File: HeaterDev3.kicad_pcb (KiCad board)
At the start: 2 copper layers, 101.6 x 76.2 mm, 27 parts, among them J1 USB_C_Receptacle_USB2.0, J9 Conn_01x04_Female, Q1 Q_NMOS_GSD, SW1 SW_SPST, U1 ATSAMD21E18A-MU, U2 FUSB302BMPX, U3 STS-30-DIS, U5 AP2112K-3.3

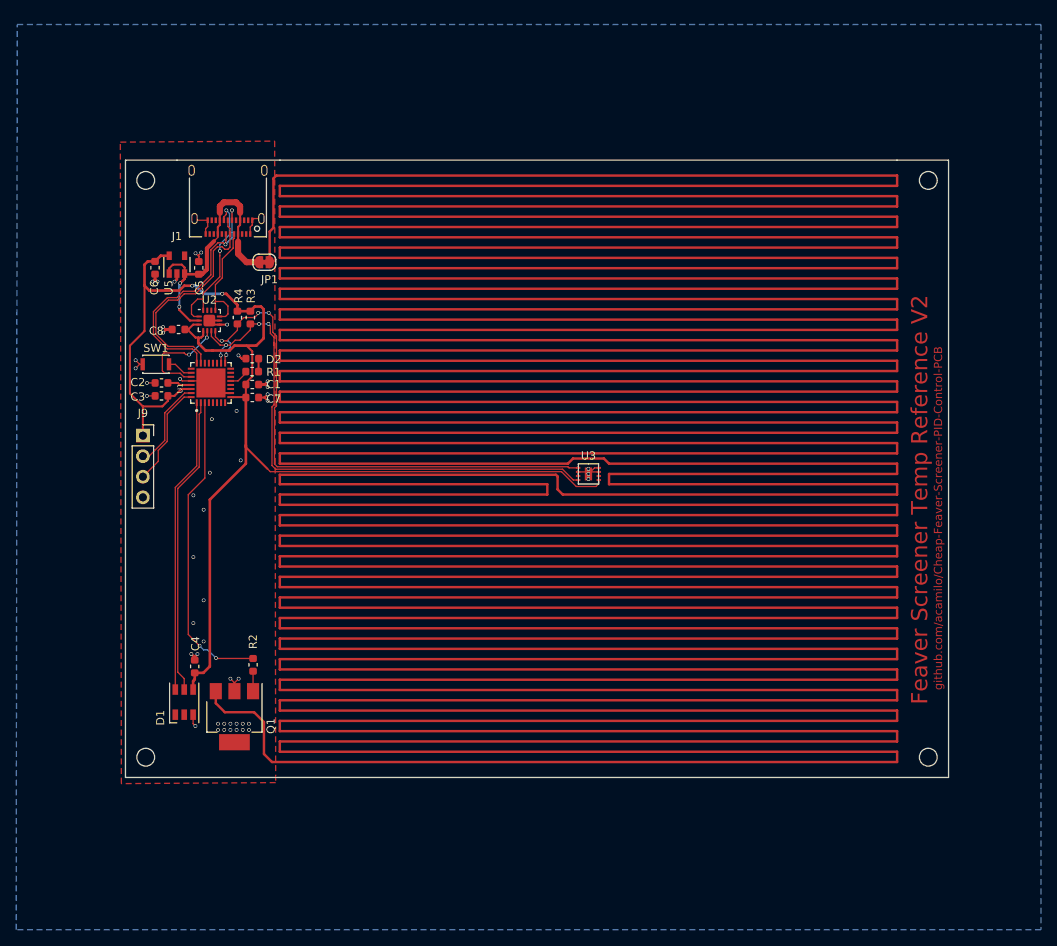
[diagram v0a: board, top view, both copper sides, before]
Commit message: Added cutout for thermal isolation.
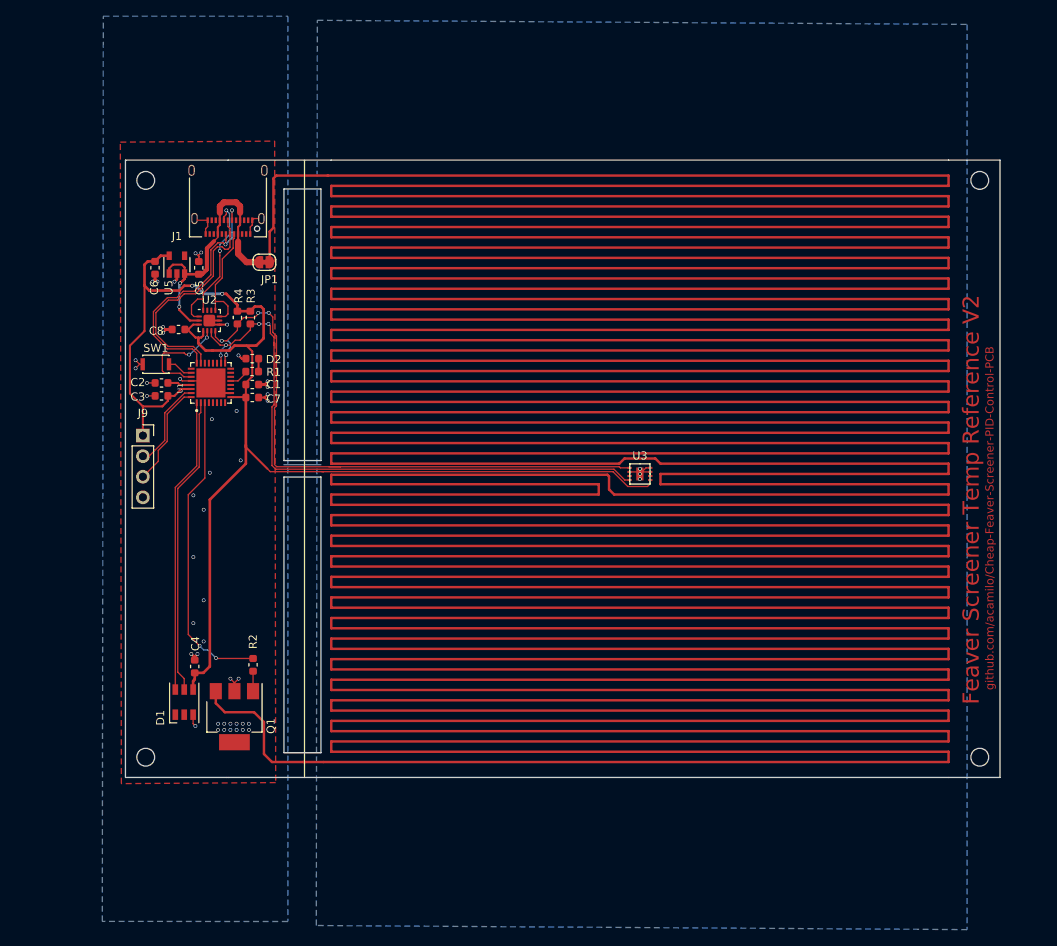
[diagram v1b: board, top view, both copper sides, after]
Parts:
- moved U3 6.35 mm to (-31.8, -37.5)
- moved H2 6.35 mm to (10.2, -2.50)
- moved H4 6.35 mm to (10.2, -73.7)
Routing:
- net /COIL: track 4507.8 -> 4520.5 mm
- net SDA_PD: track 70.6 -> 78.5 mm
- net +3V3: track 172.8 -> 179.4 mm
- net SCL_PD: track 69.0 -> 75.4 mm
- net GND: track 45.1 -> 49.7 mm
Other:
- board size 101.6 x 76.2 mm -> 108 x 76.2 mm

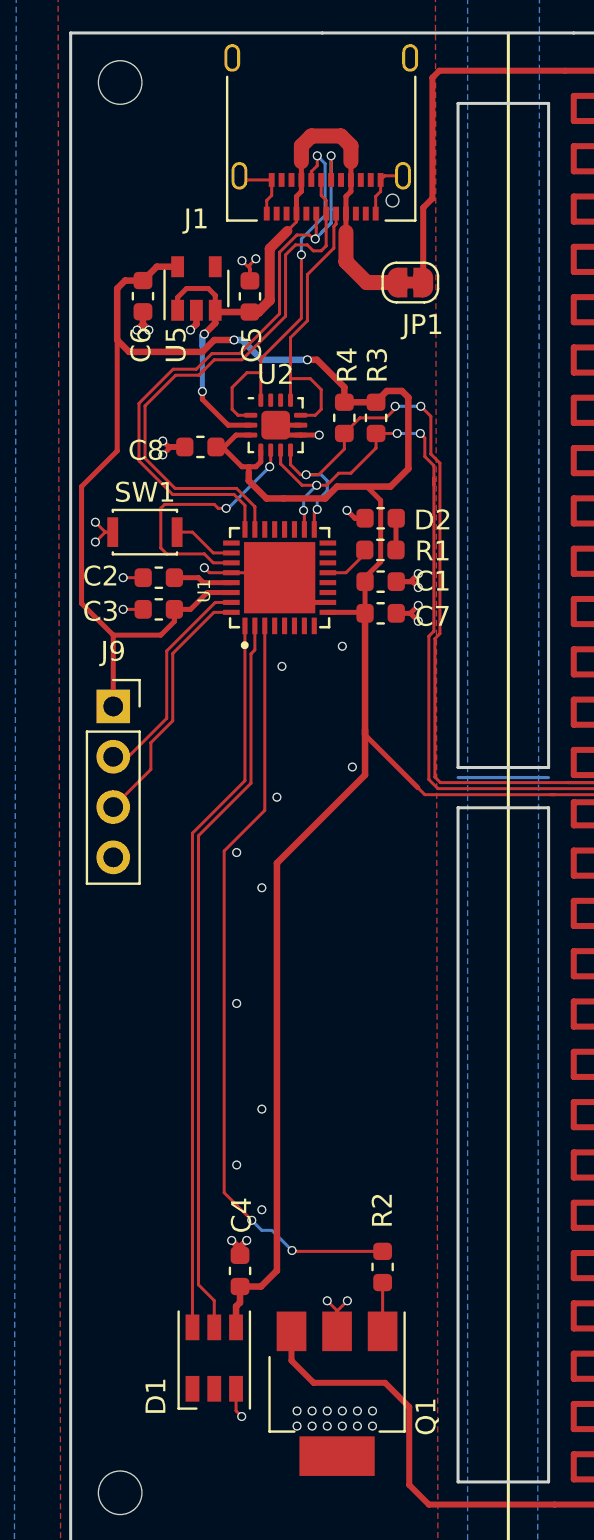
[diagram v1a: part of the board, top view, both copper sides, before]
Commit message: Fixes and changes
Swapped USB
Changed heater to PA19
Removed APA102 and replaced with SK6812MINI on pin PA06
Changed soldermask clearence
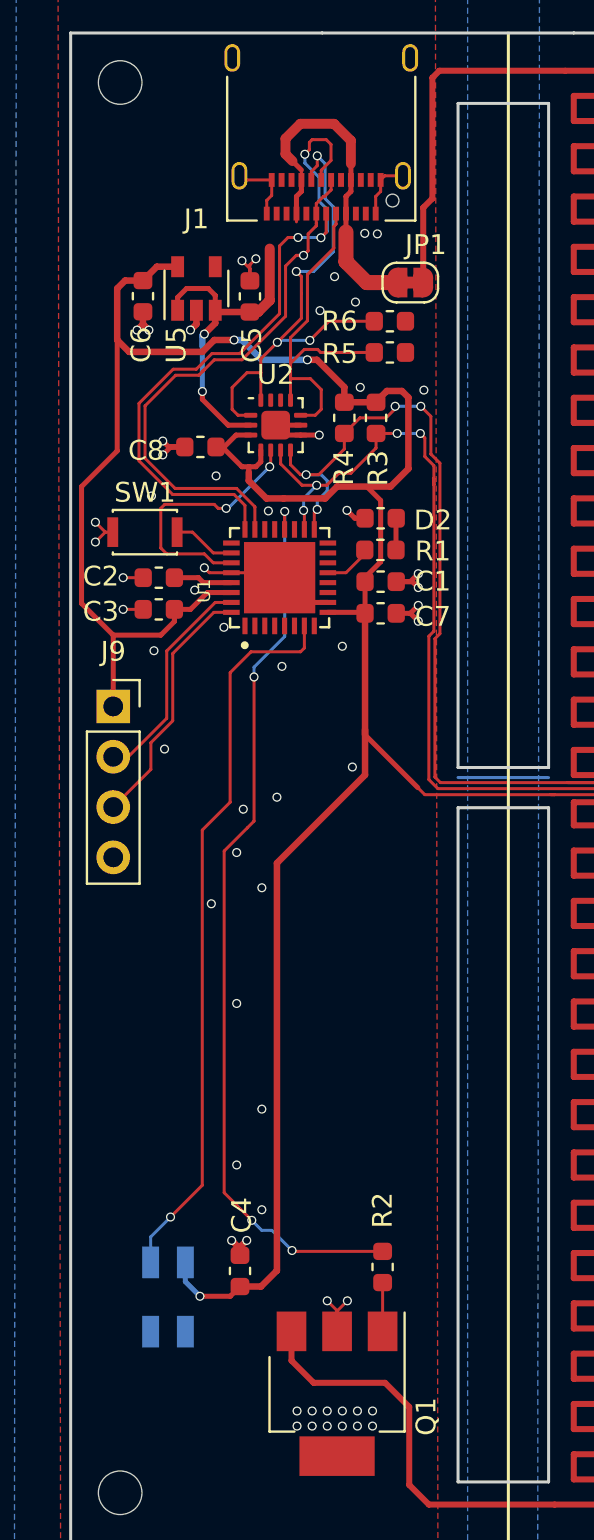
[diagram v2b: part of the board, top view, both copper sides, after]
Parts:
- added R5: 5.1k, Resistor_SMD:R_0603_1608Metric, F.Cu at (-79.1, -60.1)
- added R6: 5.1k, Resistor_SMD:R_0603_1608Metric, F.Cu at (-79.1, -61.6)
- D1: value APA102 -> SK6812MINI; footprint LED_SMD:LED_RGB_PLCC-6 -> LED_SMD:LED_SK6812MINI_PLCC4_3.5x3.5mm_P1.75mm; moved to B.Cu
- moved D1 3.87 mm to (-90.3, -12.4)
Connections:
- D1 pad 2: Net-(D1-Pad2) -> GND
- D1 pad 3: GND -> NEOPIX_DAT
- J1 pad A6: D- -> D+
- J1 pad A7: D+ -> D-
- J1 pad B6: D- -> D+
- J1 pad B7: D+ -> D-
- U1 pad 1: Net-(D1-Pad6) -> Net-(U1-Pad1)
- U1 pad 2: Net-(D1-Pad5) -> Net-(U1-Pad2)
- U1 pad 20: Net-(U1-Pad20) -> HEATER
- U1 pad 3: HEATER -> Net-(U1-Pad3)
- U1 pad 7: Net-(U1-Pad7) -> NEOPIX_DAT
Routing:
- net Net-(D1-Pad5): track 36.9 -> 0.00 mm
- net NEOPIX_DAT: track 0.00 -> 36.8 mm, vias 0 -> 1
- net Net-(D1-Pad6): track 36.5 -> 0.00 mm
- net HEATER: track 38.7 -> 45.8 mm, vias 2 -> 4
- net CC2: track 19.1 -> 25.5 mm, vias 2 -> 4
- net CC1: track 14.3 -> 19.7 mm
- net D+: track 32.5 -> 35.1 mm, vias 2 -> 3
- net +3V3: track 179.4 -> 181.5 mm, vias 2 -> 3
- net GND: track 49.7 -> 48.2 mm, vias 48 -> 63
- net D-: track 28.5 -> 27.5 mm, vias 0 -> 1
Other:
- rule pad_to_mask_clearance: 0.0762 -> 0.01

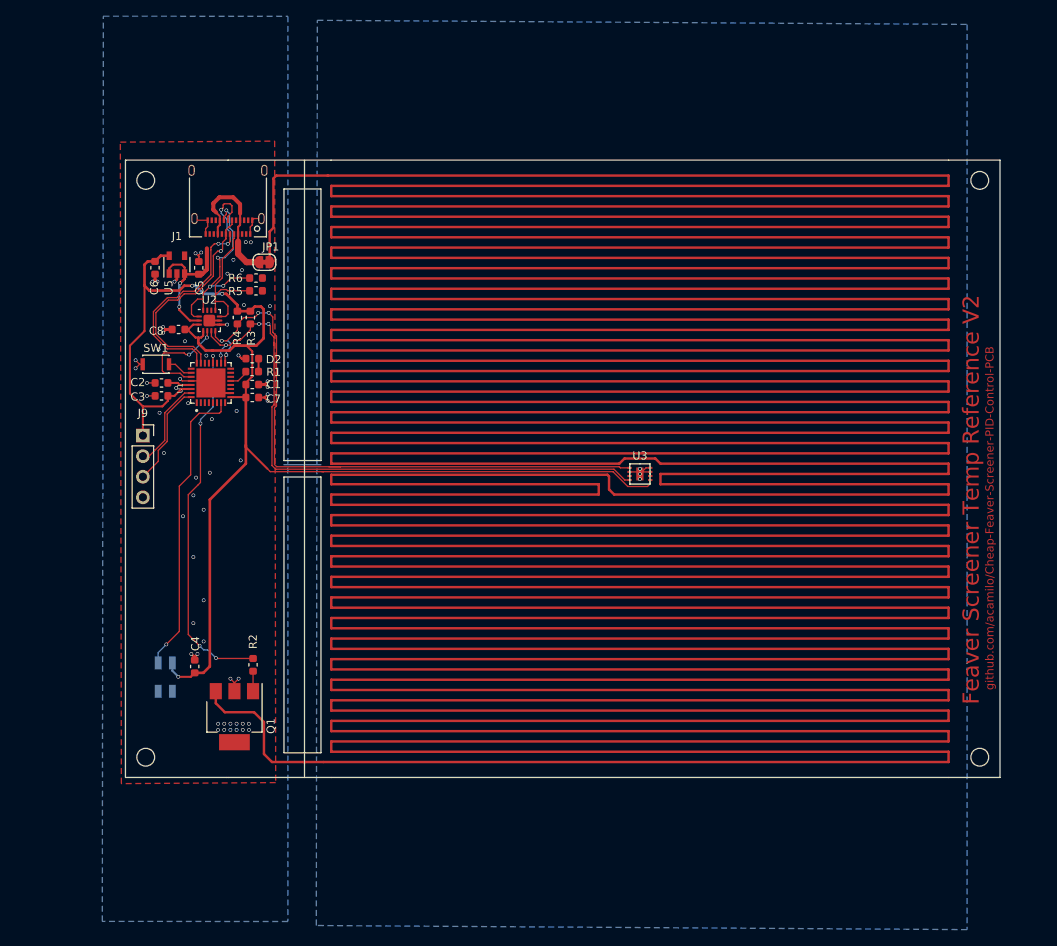
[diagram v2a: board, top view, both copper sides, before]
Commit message: Added Temperature Cutoff Circuit
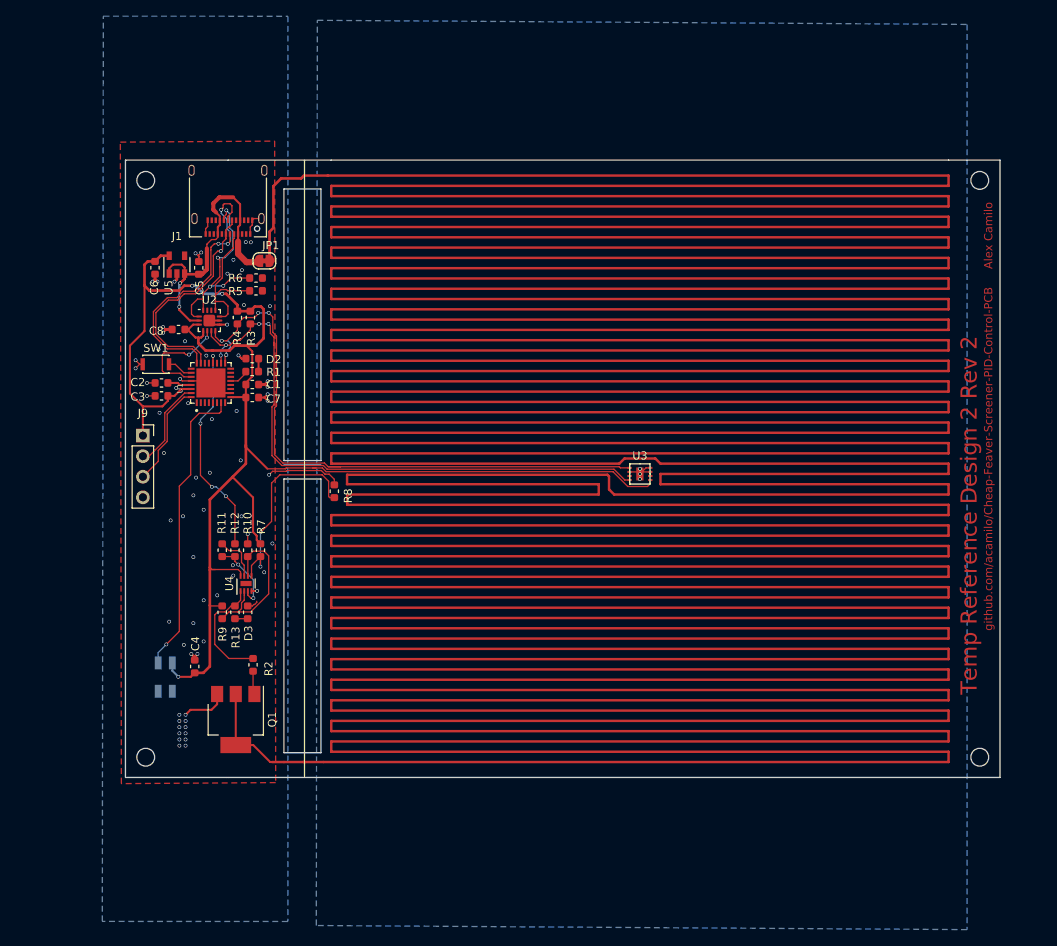
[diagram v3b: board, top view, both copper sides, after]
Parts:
- added D3: LED, Capacitor_SMD:C_0603_1608Metric, F.Cu at (-80.2, -20.4)
- added R10: 10k, Resistor_SMD:R_0603_1608Metric, F.Cu at (-80.2, -28.1)
- added R11: 10k, Resistor_SMD:R_0603_1608Metric, F.Cu at (-83.3, -28.1)
- added R12: 10k, Resistor_SMD:R_0603_1608Metric, F.Cu at (-81.7, -28.1)
- added R13: 1.5k, Resistor_SMD:R_0603_1608Metric, F.Cu at (-81.7, -20.4)
- added R7: 4.7k, Resistor_SMD:R_0603_1608Metric, F.Cu at (-78.6, -28.1)
- added R8: NTC, Resistor_SMD:R_0603_1608Metric, F.Cu at (-69.5, -35.3)
- added R9: 4.7k, Resistor_SMD:R_0603_1608Metric, F.Cu at (-83.3, -20.4)
- added U4: LM393, Package_DFN_QFN:DFN-8-1EP_2x2mm_P0.45mm_EP0.64x1.38mm, F.Cu at (-80.4, -23.9)
- Q1: value Q_NMOS_GSD -> Q_NMOS_GDS
- R3, R4: value 1.5k -> 10k
- moved Q1 0.39 mm to (-81.6, -7.15)
- moved JP1 0.17 mm to (-78.1, -63.8)
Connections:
- Q1 pad 2: GND -> /COIL
- Q1 pad 3: /COIL -> GND
- R2 pad 2: HEATER -> ELEMENT_GATE
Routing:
- net Net-(R7-Pad2): track 0.00 -> 25.4 mm, vias 0 -> 2
- net Net-(R10-Pad2): track 0.00 -> 20.2 mm
- net HEATER: track 45.8 -> 26.8 mm
- net +3V3: track 181.5 -> 198.2 mm
- net ELEMENT_GATE: track 0.00 -> 14.2 mm
- net GND: track 48.2 -> 61.4 mm, vias 63 -> 71
- net Net-(R11-Pad1): track 0.00 -> 8.98 mm, vias 0 -> 2
- net Net-(R11-Pad2): track 0.00 -> 5.86 mm
- net /COIL: track 4520.5 -> 4515.2 mm
- net VBUS: track 35.1 -> 37.3 mm
- net Net-(D3-Pad2): track 0.00 -> 1.57 mm
- net SCL_PD: track 75.4 -> 74.7 mm
- net SDA_PD: track 78.5 -> 77.7 mm
- net (no net): vias 0 -> 2
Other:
- outline, holes or cut-outs redrawn
- board text added: "Temp Reference Design 2 Rev 2"
- board text added: "github.com/acamilo/Cheap-Feaver-Screener-PID-Control-PCB Alex Camilo"
- board text removed: "Feaver Screener Temp Reference V2"
- board text removed: "github.com/acamilo/Cheap-Feaver-Screener-PID-Control-PCB"
